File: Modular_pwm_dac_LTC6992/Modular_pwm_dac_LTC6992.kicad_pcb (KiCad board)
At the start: 2 copper layers, 48.3 x 12.6 mm, 15 parts, among them J2 Screw_Terminal_01x02, J3 Conn_01x03_Male, J4 Conn_01x03_Male, U1 LTC6992-1 (Rev. D)

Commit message: Finished All
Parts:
- added J3: Conn_01x03_Male, Connector_PinHeader_2.54mm:PinHeader_1x03_P2.54mm_Vertical, F.Cu at (157.9, 41.7)
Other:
- board size 48.3 x 12.6 mm -> 52.8 x 12.6 mm
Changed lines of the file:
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@@
     (tracks 53)
     (zones 0)
-    (modules 15)
+    (modules 16)
     (nets 10)
   )
   (page A4)
   (layers
-    (0 F.Cu signal hide)
-    (31 B.Cu signal hide)
+    (0 F.Cu signal)
+    (31 B.Cu signal)
     (32 B.Adhes user)
     (33 F.Adhes user)
@@
   )
   (module Connector_PinHeader_2.54mm:PinHeader_1x03_P2.54mm_Vertical (layer F.Cu)
+    (at 157.9245 41.656)
+    (descr "Through hole straight pin header, 1x03, 2.54mm pitch, single row")
+    (tags "Through hole pin header THT 1x03 2.54mm single row")
+    (fp_text reference J3 (at -2.286 -1.016) (layer F.SilkS)
+      (effects (font (size 1 1) (thickness 0.15)))
+    )
+    (fp_text value Conn_01x03_Male (at 0 7.41) (layer F.Fab)
+      (effects (font (size 1 1) (thickness 0.15)))
+    )
+    (fp_line (start -0.635 -1.27) (end 1.27 -1.27) (layer F.Fab) (width 0.1))
+    (fp_line (start 1.27 -1.27) (end 1.27 6.35) (layer F.Fab) (width 0.1))
+    (fp_line (start 1.27 6.35) (end -1.27 6.35) (layer F.Fab) (width 0.1))
+    (fp_line (start -1.27 6.35) (end -1.27 -0.635) (layer F.Fab) (width 0.1))
+    (fp_line (start -1.27 -0.635) (end -0.635 -1.27) (layer F.Fab) (width 0.1))
+    (fp_line (start -1.33 6.41) (end 1.33 6.41) (layer F.SilkS) (width 0.12))
+    (fp_line (start -1.33 1.27) (end -1.33 6.41) (layer F.SilkS) (width 0.12))
+    (fp_line (start 1.33 1.27) (end 1.33 6.41) (layer F.SilkS) (width 0.12))
+    (fp_line (start -1.33 1.27) (end 1.33 1.27) (layer F.SilkS) (width 0.12))
+    (fp_line (start -1.33 0) (end -1.33 -1.33) (layer F.SilkS) (width 0.12))
+    (fp_line (start -1.33 -1.33) (end 0 -1.33) (layer F.SilkS) (width 0.12))
+    (fp_line (start -1.8 -1.8) (end -1.8 6.85) (layer F.CrtYd) (width 0.05))
+    (fp_line (start -1.8 6.85) (end 1.8 6.85) (layer F.CrtYd) (width 0.05))
+    (fp_line (start 1.8 6.85) (end 1.8 -1.8) (layer F.CrtYd) (width 0.05))
+    (fp_line (start 1.8 -1.8) (end -1.8 -1.8) (layer F.CrtYd) (width 0.05))
+    (fp_text user %R (at 0 2.54 90) (layer F.Fab)
+      (effects (font (size 1 1) (thickness 0.15)))
+    )
+    (pad 3 thru_hole oval (at 0 5.08) (size 1.7 1.7) (drill 1) (layers *.Cu *.Mask))
+    (pad 2 thru_hole oval (at 0 2.54) (size 1.7 1.7) (drill 1) (layers *.Cu *.Mask)
+      (net 1 GND))
+    (pad 1 thru_hole rect (at 0 0) (size 1.7 1.7) (drill 1) (layers *.Cu *.Mask)
+      (net 2 +5V))
+    (model ${KISYS3DMOD}/Connector_PinHeader_2.54mm.3dshapes/PinHeader_1x03_P2.54mm_Vertical.wrl
+      (at (xyz 0 0 0))
+      (scale (xyz 1 1 1))
+      (rotate (xyz 0 0 0))
+    )
+  )
+  (module Connector_PinHeader_2.54mm:PinHeader_1x03_P2.54mm_Vertical (layer F.Cu)
     (at 153.289 41.656)
     (descr "Through hole straight pin header, 1x03, 2.54mm pitch, single row")
@@
     )
   )
-  (gr_line (start 156.718 38.989) (end 156.718 49.022) (layer Edge.Cuts) (width 0.05))
+  (gr_line (start 161.2265 38.989) (end 161.2265 49.022) (layer Edge.Cuts) (width 0.05))
   (gr_line (start 108.458 38.989) (end 108.458 49.022) (layer Edge.Cuts) (width 0.05))
-  (gr_line (start 109.728 37.719) (end 155.448 37.719) (layer Edge.Cuts) (width 0.05))
-  (gr_line (start 155.448 50.292) (end 109.728 50.292) (layer Edge.Cuts) (width 0.05))
+  (gr_line (start 109.728 37.719) (end 159.9565 37.719) (layer Edge.Cuts) (width 0.05))
+  (gr_line (start 159.9565 50.292) (end 109.728 50.292) (layer Edge.Cuts) (width 0.05))
   (gr_arc (start 109.728 38.989) (end 109.728 37.719) (angle -90) (layer Edge.Cuts) (width 0.05))
   (gr_arc (start 109.728 49.022) (end 108.458 49.022) (angle -90) (layer Edge.Cuts) (width 0.05))
-  (gr_arc (start 155.448 49.022) (end 155.448 50.292) (angle -90) (layer Edge.Cuts) (width 0.05))
-  (gr_arc (start 155.448 38.989) (end 156.718 38.989) (angle -90) (layer Edge.Cuts) (width 0.05))
+  (gr_arc (start 159.9565 49.022) (end 159.9565 50.292) (angle -90) (layer Edge.Cuts) (width 0.05))
+  (gr_arc (start 159.9565 38.989) (end 161.2265 38.989) (angle -90) (layer Edge.Cuts) (width 0.05))
   (gr_text PWM (at 148.844 48.895) (layer F.SilkS)
     (effects (font (size 1 1) (thickness 0.15)))
@@
     (polygon
       (pts
-        (xy 156.21 49.53) (xy 109.982 49.53) (xy 109.982 38.608) (xy 156.21 38.608)
+        (xy 160.0835 49.53) (xy 109.982 49.53) (xy 109.982 38.608) (xy 160.0835 38.608)
       )
     )
@@
     (polygon
       (pts
-        (xy 156.21 49.53) (xy 109.982 49.53) (xy 109.982 38.608) (xy 156.21 38.608)
+        (xy 160.0835 49.53) (xy 109.982 49.53) (xy 109.982 38.608) (xy 160.0835 38.608)
       )
     )

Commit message: Yes they are
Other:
- board text added: "DRIVER"
- board text added: "REGULATOR"

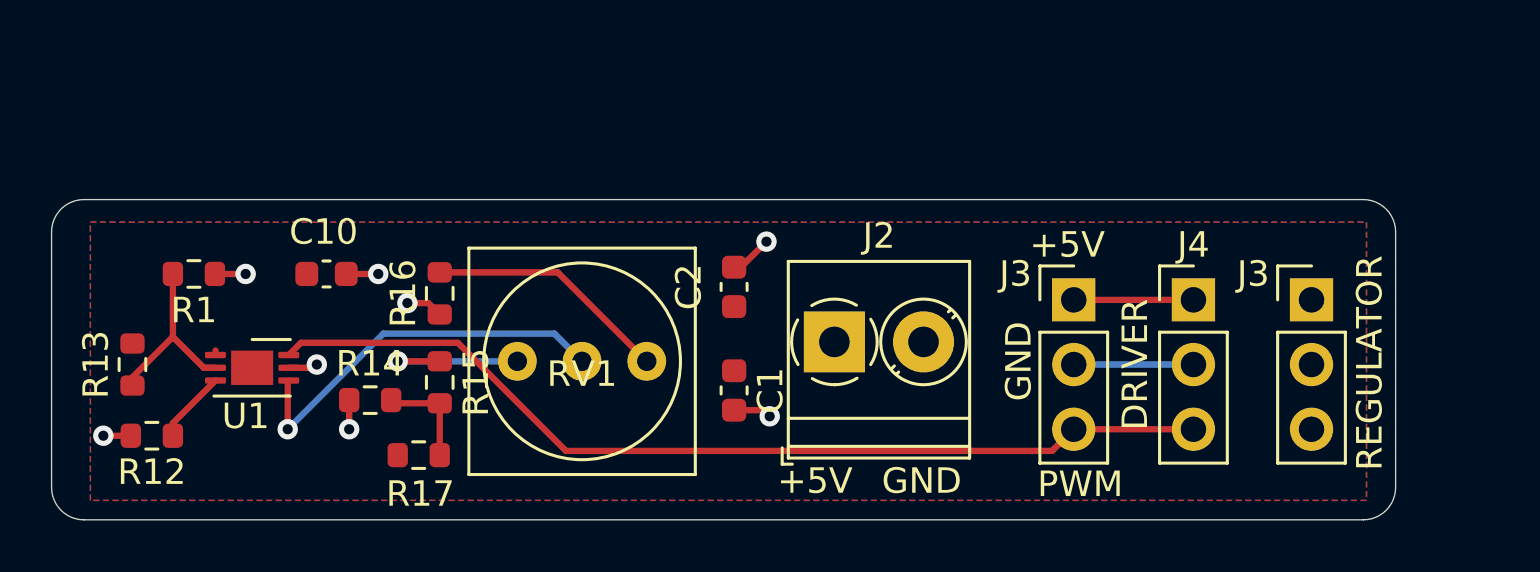
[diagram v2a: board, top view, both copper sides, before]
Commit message: NEW PCB
Changed some names of old PCBs, and created new PCB with the new package
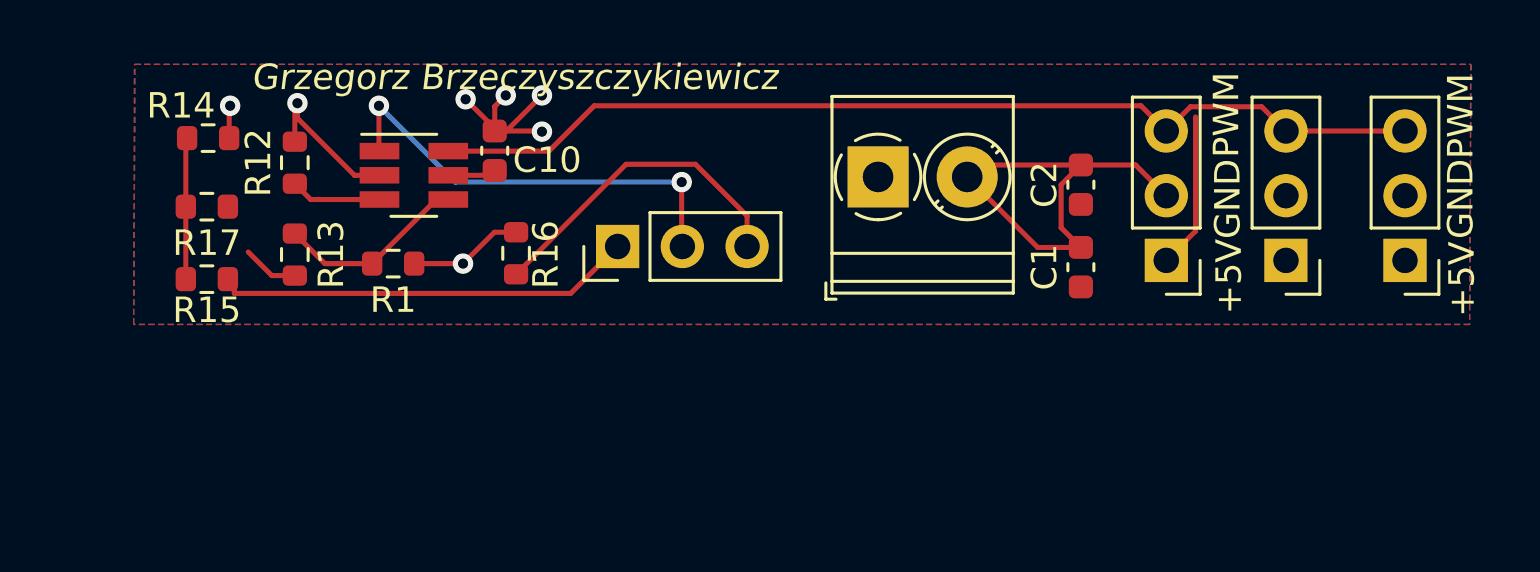
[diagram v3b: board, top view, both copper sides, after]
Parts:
- removed the J3 at (157.9, 41.7)
- removed the J3 at (148.6, 41.7)
- removed J4: Conn_01x03_Male, Connector_PinHeader_2.54mm:PinHeader_1x03_P2.54mm_Vertical
- added J3: Conn_01x03_Male, Connector_PinHeader_2.54mm:PinHeader_1x03_P2.54mm_Vertical, F.Cu at (161.6, 40.1)
- added J3: Conn_01x03_Male, Connector_PinHeader_2.54mm:PinHeader_1x03_P2.54mm_Vertical, F.Cu at (156.9, 40.1)
- added J3: Conn_01x03_Male, Connector_PinHeader_2.54mm:PinHeader_1x03_P2.54mm_Vertical, F.Cu at (152.2, 40.1)
- RV1: footprint HS2_parts:oldpot -> Connector_PinHeader_2.54mm:PinHeader_1x03_P2.54mm_Vertical
- U1: footprint Package_DFN_QFN:DFN-6-1EP_3x2mm_P0.5mm_EP1.65x1.35mm -> Package_TO_SOT_SMD:SOT-23-6_Handsoldering
- moved C1 14.4 mm to (148.9, 40.4), turned to 90 degrees
- moved C2 14.2 mm to (148.9, 37.1)
- moved R17 12.8 mm to (114.6, 38.0), turned to 180 degrees
- moved R12 12.1 mm to (118.0, 36.3), turned to 90 degrees
- moved R14 12.1 mm to (114.6, 35.3), turned to 180 degrees
- moved R15 10.0 mm to (114.6, 40.8), turned to 180 degrees
- moved U1 9.87 mm to (122.7, 36.8)
- moved C10 8.19 mm to (125.9, 35.8), turned to 270 degrees
- moved R1 7.83 mm to (121.9, 40.2)
- moved R13 7.70 mm to (118.0, 39.9), turned to 270 degrees
- moved J2 6.70 mm to (140.9, 36.8)
- moved RV1 4.72 mm to (130.7, 39.6), turned to 90 degrees
- moved R16 3.39 mm to (126.7, 39.8), turned to 270 degrees
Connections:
- U1 pad 1: +5V -> /IN
- U1 pad 2: Net-(R1-Pad2) -> GND
- U1 pad 4: /IN -> Net-(R1-Pad2)
- U1 pad 5: GND -> +5V
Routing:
- net GND: track 15.2 -> 37.9 mm, vias 8 -> 7
- net Net-(R15-Pad1): track 6.35 -> 17.5 mm, vias 1 -> 0
- net +5V: track 4.87 -> 10.2 mm
- net Net-(R16-Pad2): track 9.57 -> 12.9 mm
- net /IN: track 15.5 -> 17.5 mm, vias 1 -> 2
- net /PWM: track 37.8 -> 39.5 mm
- net Net-(R14-Pad2): track 3.99 -> 5.56 mm
- net Net-(R12-Pad1): track 2.86 -> 3.75 mm
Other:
- board outline removed
- net class Default: trace_width 0.25 -> 0.2
- board text added: "Grzegorz Brzeczyszczykiewicz"
- board text removed: "DRIVER"
- board text removed: "REGULATOR"
